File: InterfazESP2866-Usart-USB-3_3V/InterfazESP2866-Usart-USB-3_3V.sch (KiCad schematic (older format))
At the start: 12 parts, among them P1 USB_USART, P2 ESP2866, P3 Flash, U1 LM1084IS-ADJ/NOPB

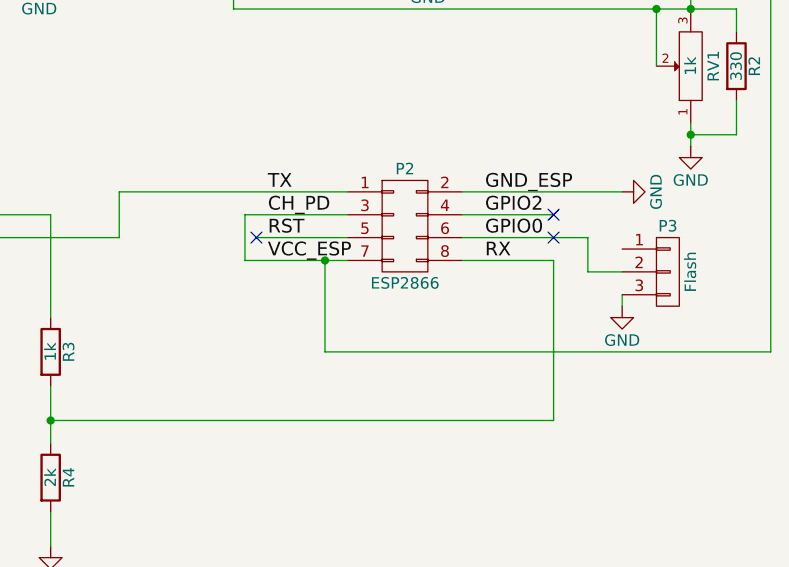
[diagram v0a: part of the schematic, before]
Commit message: Terminado de rutear interfaz usart usb
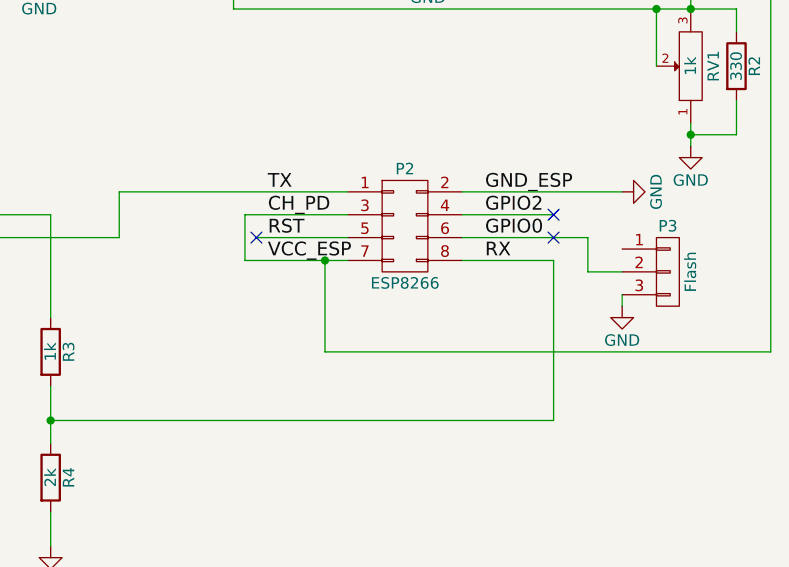
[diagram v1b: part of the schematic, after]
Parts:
- P2: value ESP2866 -> ESP8266
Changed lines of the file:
@@
 P 5200 2800
 F 0 "P2" H 5200 3050 50  0000 C CNN
-F 1 "ESP2866" H 5200 2550 50  0000 C CNN
+F 1 "ESP8266" H 5200 2550 50  0000 C CNN
 F 2 "Pin_Headers:Pin_Header_Straight_2x04" H 5200 1600 60  0001 C CNN
 F 3 "" H 5200 1600 60  0000 C CNN
